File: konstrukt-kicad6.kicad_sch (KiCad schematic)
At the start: 0 parts

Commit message: LFO schem init
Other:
- added sheet LFO (lfo.kicad_sch)

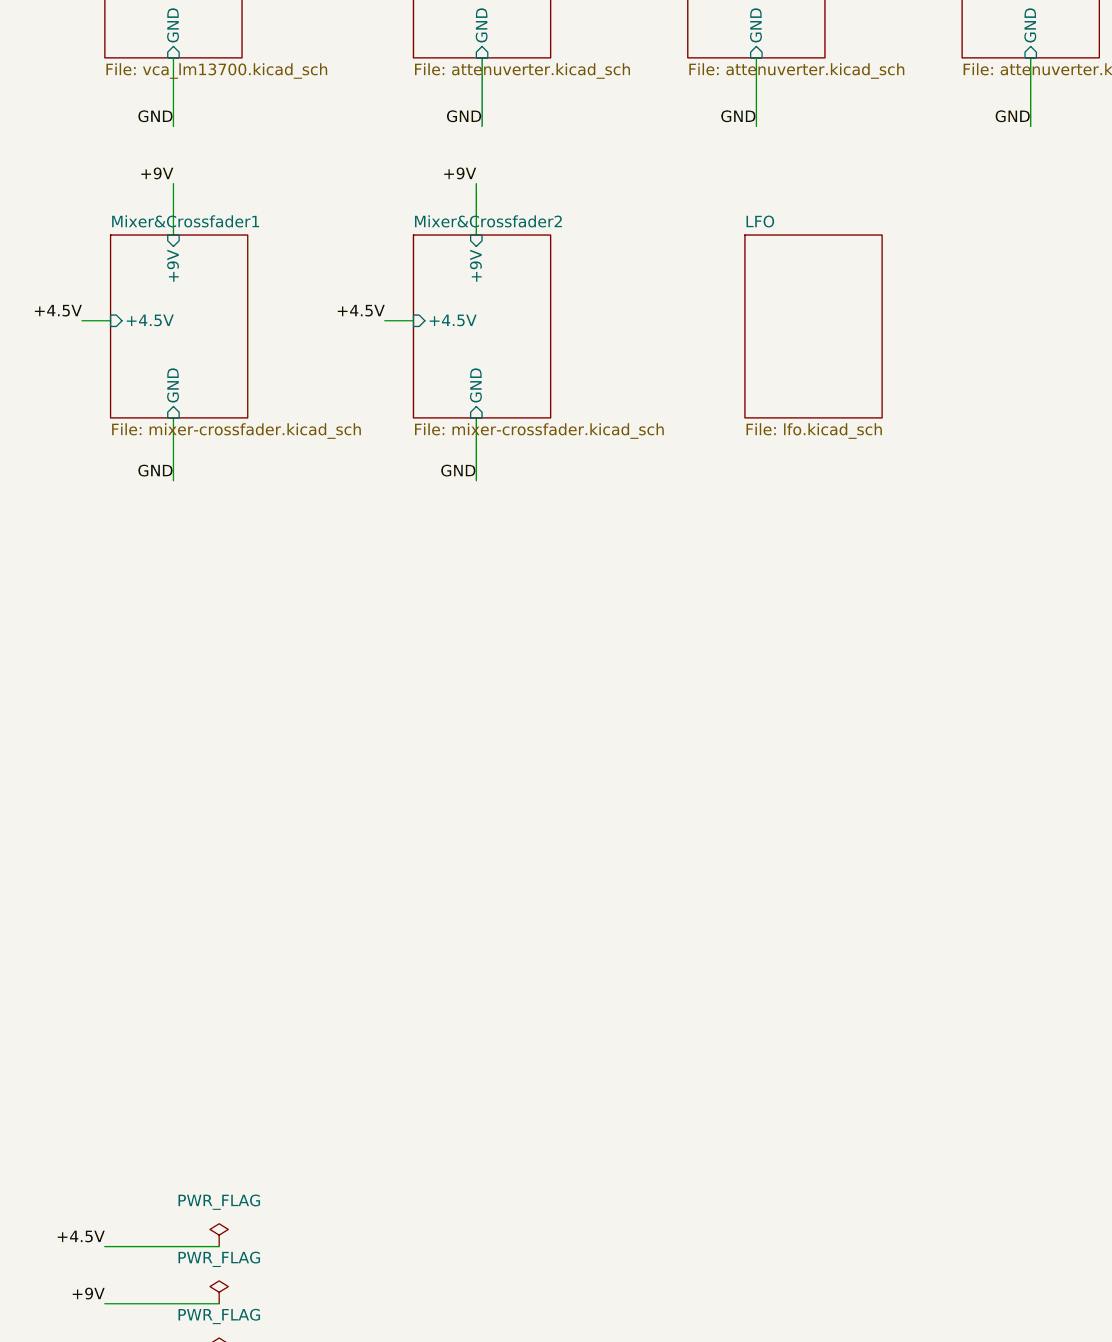
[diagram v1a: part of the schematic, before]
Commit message: LFO schem capture done / replace r2r opamps
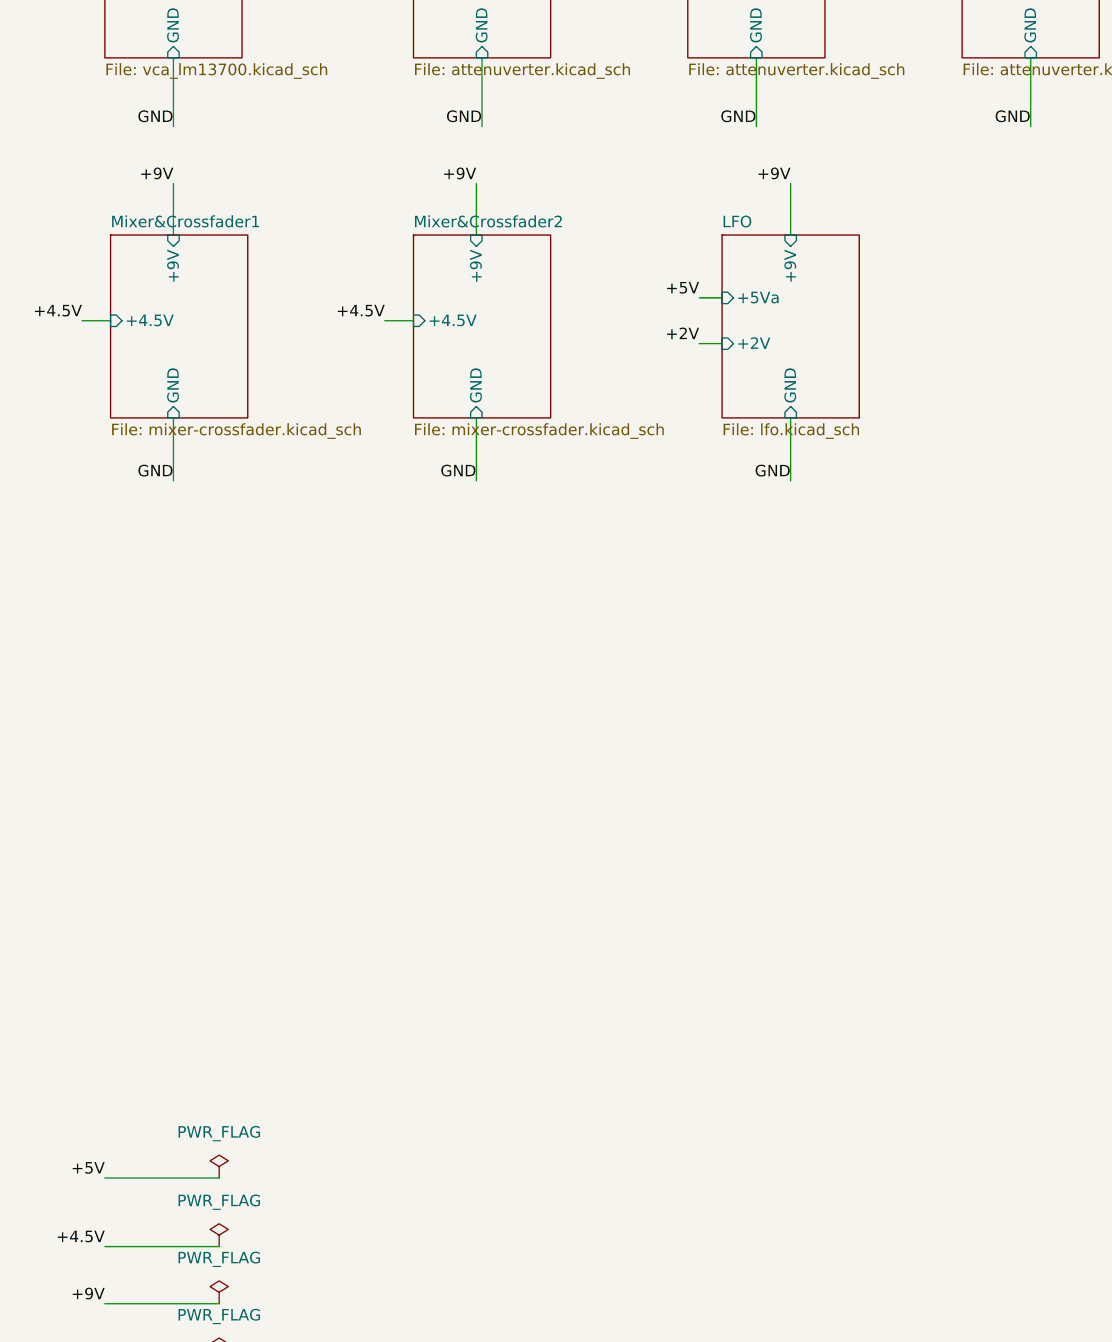
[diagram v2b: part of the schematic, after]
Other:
- sheet LFO ports: added +2V, +5Va, +9V, GND; removed none

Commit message: Relay switch schem capture done
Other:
- added sheet Relay switch (relay-switch.kicad_sch)

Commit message: Relay switch layout done
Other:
- sheet Relay switch ports: added +9V, GND; removed none

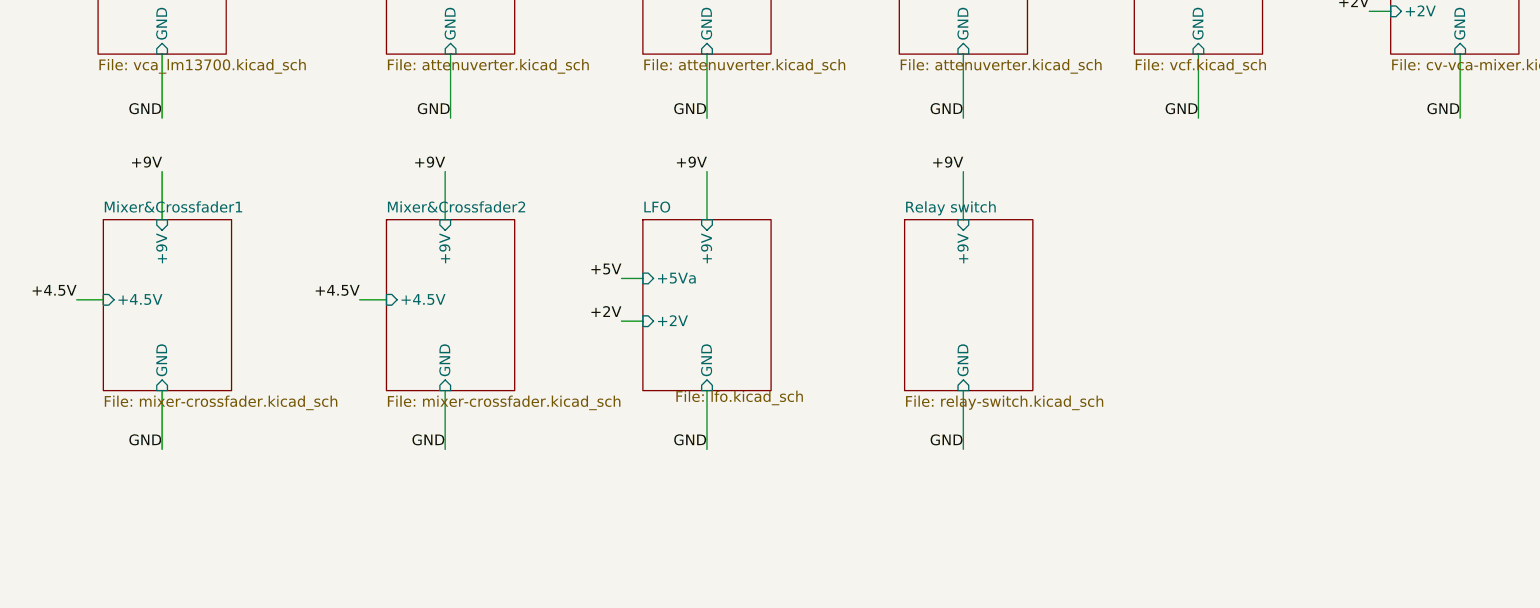
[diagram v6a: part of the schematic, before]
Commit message: Tone control schematic & layout
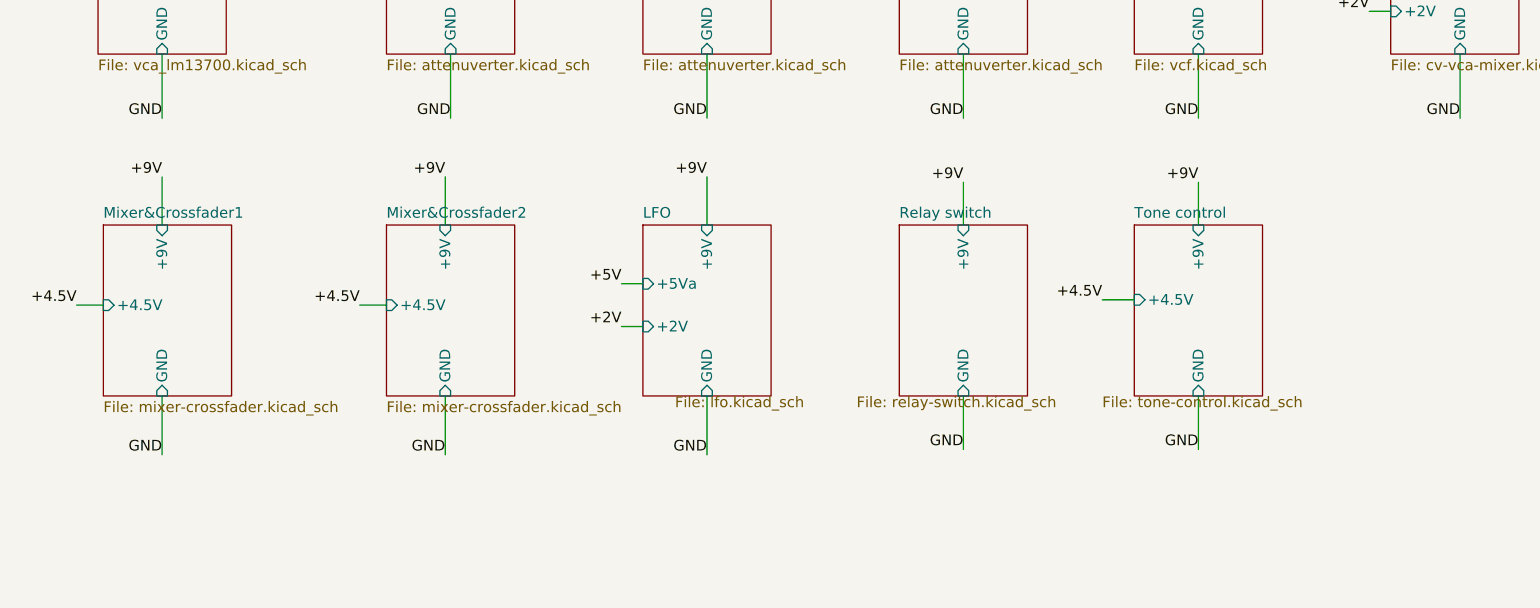
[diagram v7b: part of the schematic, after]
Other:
- added sheet Tone control (tone-control.kicad_sch)

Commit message: VC-limiter schem & layout
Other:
- added sheet VC Limiter (vc-limiter.kicad_sch)
